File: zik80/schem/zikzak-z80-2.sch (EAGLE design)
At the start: 66 parts, among them IC1 Z80, IC10 74LS32N, IC11 74LS32N, IC12 74LS32N, IC13 74LS32N, IC14 74LS04N, IC15 74LS32N, IC16 ATMEGA644-20PU, IC2 ATMEGA644-20PU, IC3 MC6850, IC4 74LS32N, IC5 74LS04N, IC6 74LS32N, U2 FT232RLSSOP, X2 USB-SMD-NS

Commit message: Schematic update
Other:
- note added: "TODO: Check if VBL is needed.. VSYNC may be sufficient, and can be connected to both VGA and to IO mcu.. --> free a pin!"
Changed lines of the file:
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@@
 <setting verticaltext="up"/>
 </settings>
-<grid distance="0.05" unitdist="inch" unit="inch" style="dots" multiple="1" display="yes" altdistance="0.01" altunitdist="inch" altunit="inch"/>
+<grid distance="0.1" unitdist="inch" unit="inch" style="lines" multiple="1" display="no" altdistance="0.01" altunitdist="inch" altunit="inch"/>
 <layers>
 <layer number="1" name="Top" color="4" fill="1" visible="no" active="no"/>
@@
 <rectangle x1="3.81" y1="109.22" x2="35.56" y2="135.89" layer="203"/>
 <text x="6.35" y="138.43" size="5.08" layer="91">ISP Progr. IO</text>
+<text x="478.79" y="40.64" size="3.81" layer="94">TODO: Check if VBL is needed..
+VSYNC may be sufficient, and can be
+connected to both VGA and to IO mcu..
+--&gt; free a pin!</text>
 </plain>
 <instances>

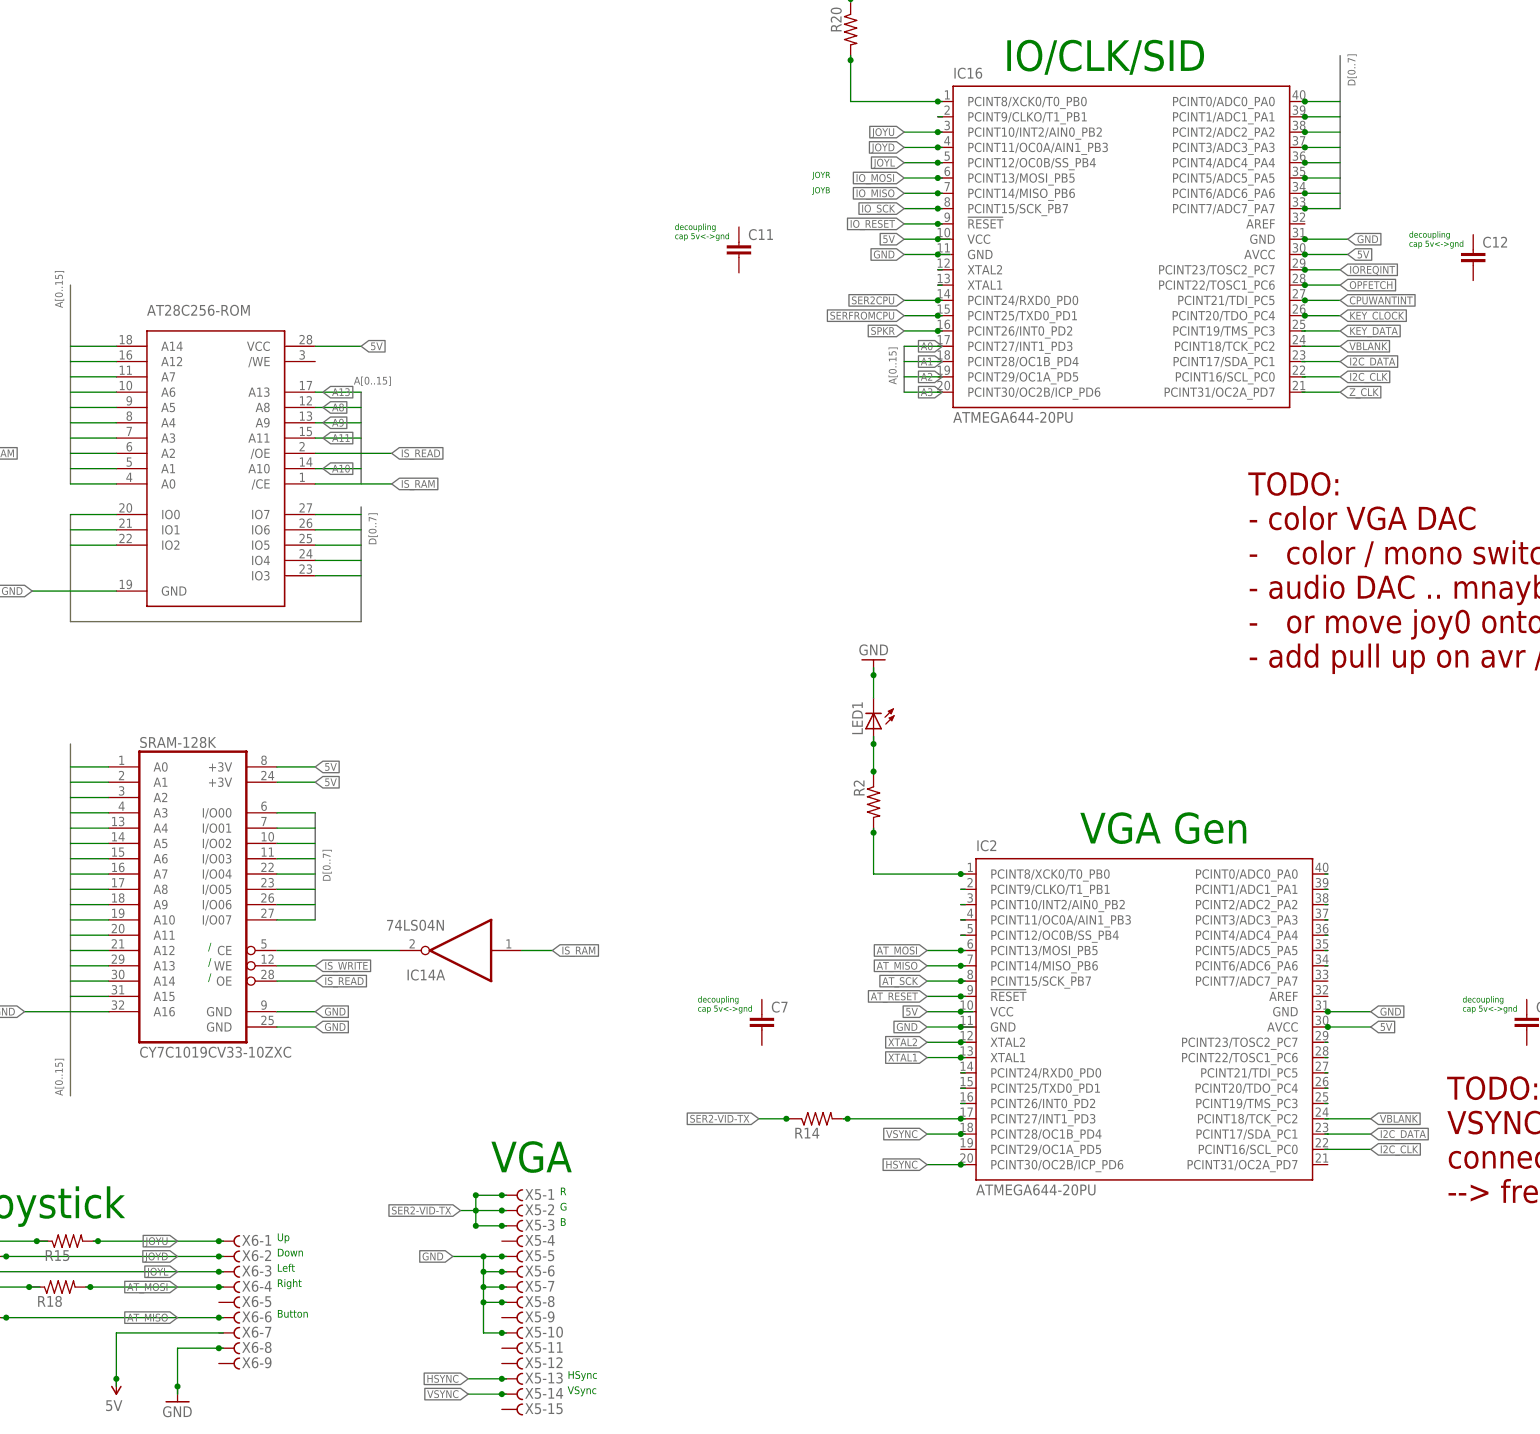
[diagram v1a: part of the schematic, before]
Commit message: Added skeleton for '3w' 3-wire-interface, but not using it; updated schem to move VGA stuff more to one side, opening up full side for something else..
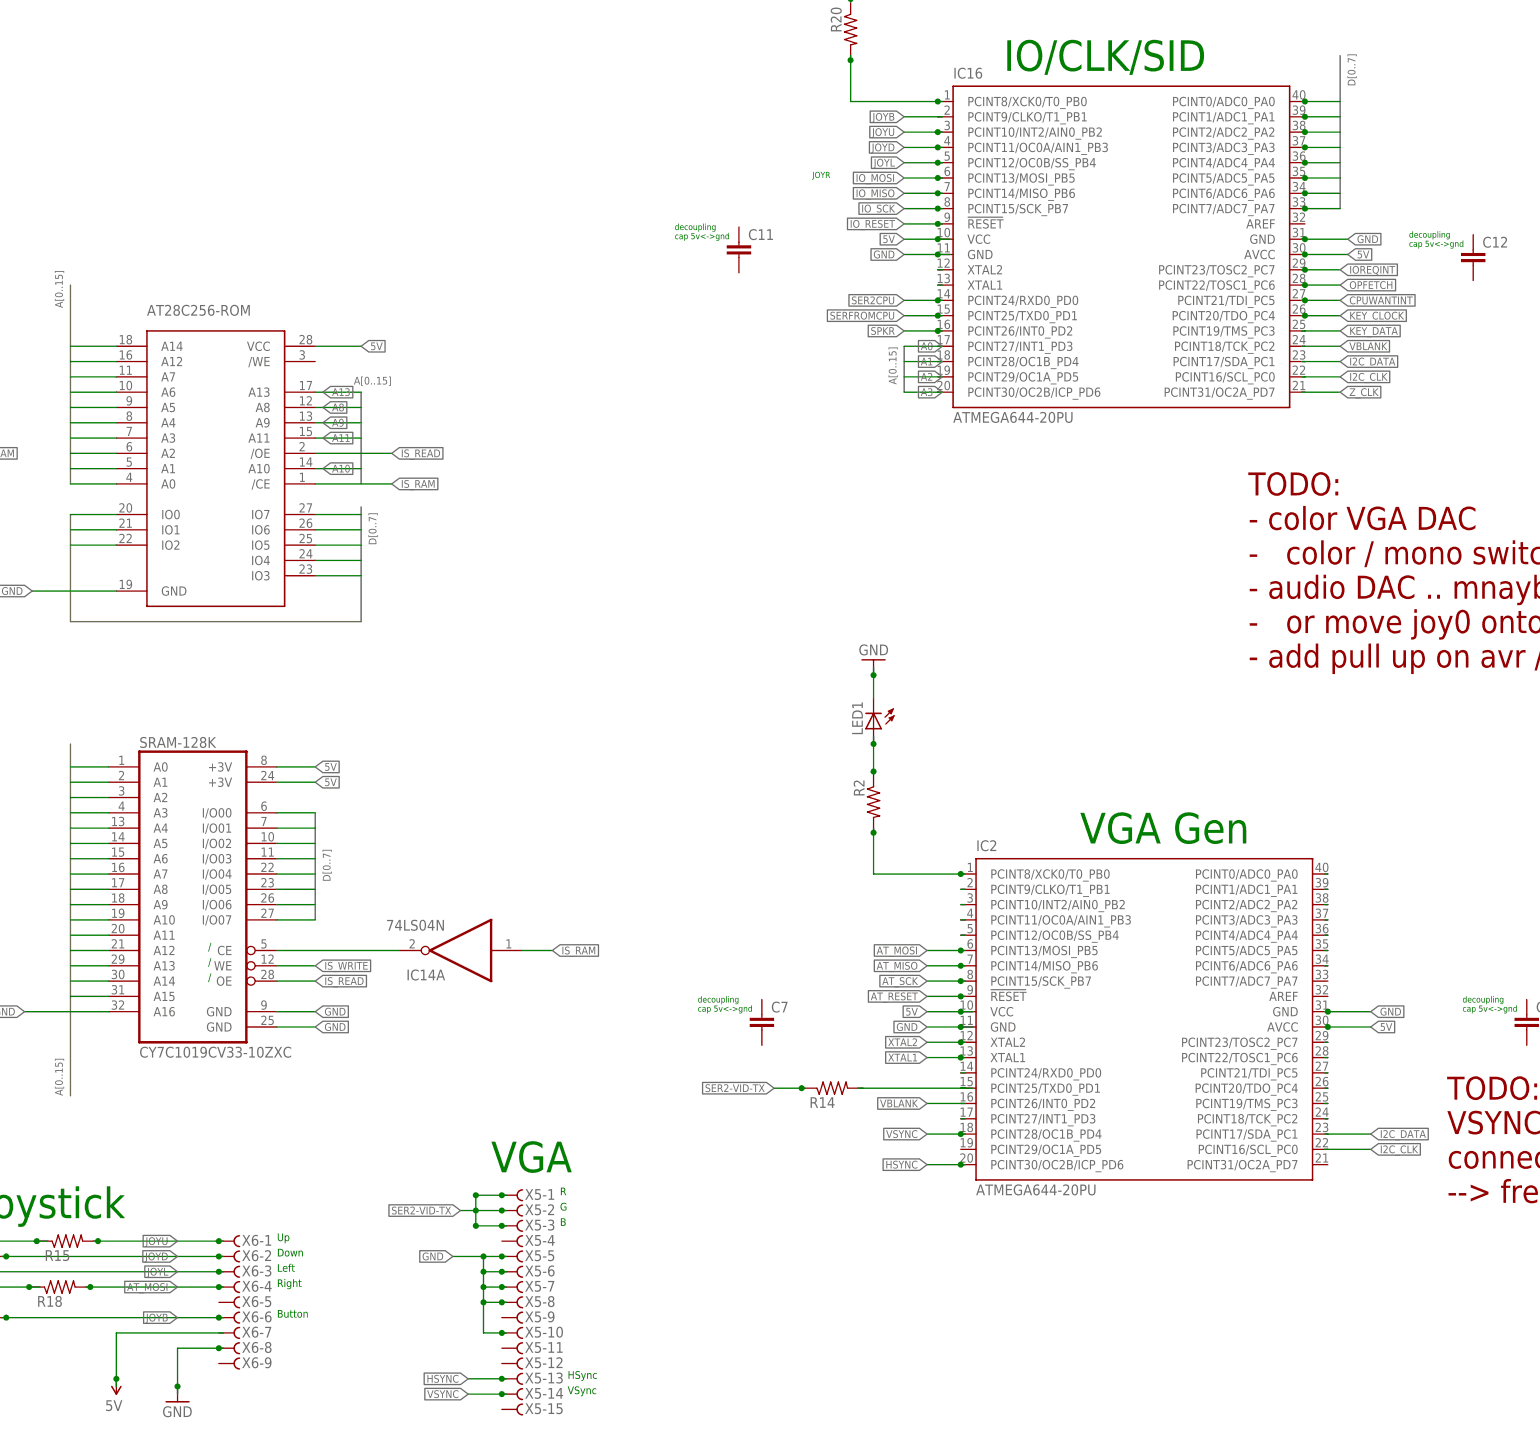
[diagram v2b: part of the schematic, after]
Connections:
- removed net N$13: IC16.PCINT8/XCK0/T0_PB0, R20.2
- new net JOYB: IC16.PCINT8/XCK0/T0_PB0, IC16.PCINT9/CLKO/T1_PB1, R19.2, R20.2, X6-6.F
- new net N$3: R14.2
- net AT_MISO: no longer R19.2, X6-6.F
- net CPUWANTINT: no longer IC16.PCINT9/CLKO/T1_PB1
- net N$10: no longer R14.2
- net SERFROMCPU: no longer IC2.PCINT25/TXD0_PD1
- net SPKR: no longer IC2.PCINT26/INT0_PD2
- net VBLANK: now also IC2.PCINT25/TXD0_PD1, IC2.PCINT26/INT0_PD2
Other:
- note removed: "JOYB"
- moved on the sheet: R14
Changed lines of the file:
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@@
 <setting verticaltext="up"/>
 </settings>
-<grid distance="0.1" unitdist="inch" unit="inch" style="lines" multiple="1" display="no" altdistance="0.01" altunitdist="inch" altunit="inch"/>
+<grid distance="0.05" unitdist="inch" unit="inch" style="dots" multiple="1" display="yes" altdistance="0.01" altunitdist="inch" altunit="inch"/>
 <layers>
 <layer number="1" name="Top" color="4" fill="1" visible="no" active="no"/>
@@
 cap 5v&lt;-&gt;gnd</text>
 <text x="373.38" y="210.82" size="1.016" layer="91">JOYR</text>
-<text x="373.38" y="208.28" size="1.016" layer="91">JOYB</text>
 <text x="472.44" y="199.39" size="1.016" layer="91">decoupling
 cap 5v&lt;-&gt;gnd</text>
@@
 <instance part="GND11" gate="1" x="78.74" y="8.89"/>
 <instance part="GND12" gate="1" x="93.98" y="8.89"/>
-<instance part="R14" gate="G$1" x="374.142" y="54.61" rot="MR180"/>
+<instance part="R14" gate="G$1" x="376.682" y="59.69" rot="MR180"/>
 <instance part="X6" gate="-1" x="277.368" y="34.29"/>
 <instance part="X6" gate="-2" x="277.368" y="31.75"/>
@@
 </segment>
 <segment>
-<wire x1="398.78" y1="59.69" x2="398.018" y2="59.69" width="0.1524" layer="91"/>
-<pinref part="IC2" gate="G$1" pin="PCINT25/TXD0_PD1"/>
-</segment>
-<segment>
 <wire x1="394.97" y1="187.96" x2="394.208" y2="187.96" width="0.1524" layer="91"/>
 <label x="388.62" y="187.96" size="1.27" layer="95" rot="R180" xref="yes"/>
@@
 <junction x="398.018" y="80.01"/>
 </segment>
-<segment>
-<wire x1="275.59" y1="21.59" x2="274.828" y2="21.59" width="0.1524" layer="91"/>
-<label x="267.97" y="21.59" size="1.27" layer="95" rot="R180" xref="yes"/>
-<wire x1="274.828" y1="21.59" x2="239.522" y2="21.59" width="0.1524" layer="91"/>
-<pinref part="X6" gate="-6" pin="F"/>
-<junction x="274.828" y="21.59"/>
-<pinref part="R19" gate="G$1" pin="2"/>
-<wire x1="239.522" y1="21.59" x2="238.76" y2="21.59" width="0.1524" layer="91"/>
-<junction x="239.522" y="21.59"/>
-</segment>
 </net>
 <net name="+5V" class="0">
@@
 </segment>
 <segment>
-<wire x1="394.97" y1="220.98" x2="394.208" y2="220.98" width="0.1524" layer="91"/>
-<pinref part="IC16" gate="G$1" pin="PCINT9/CLKO/T1_PB1"/>
-</segment>
-<segment>
 <wire x1="454.66" y1="190.5" x2="455.168" y2="190.5" width="0.1524" layer="91"/>
 <label x="461.01" y="190.5" size="1.27" layer="95" xref="yes"/>
@@
 <net name="N$10" class="0">
 <segment>
-<wire x1="378.46" y1="54.61" x2="379.222" y2="54.61" width="0.1524" layer="91"/>
 <pinref part="IC2" gate="G$1" pin="PCINT27/INT1_PD3"/>
-<wire x1="379.222" y1="54.61" x2="398.018" y2="54.61" width="0.1524" layer="91"/>
 <wire x1="398.018" y1="54.61" x2="398.78" y2="54.61" width="0.1524" layer="91"/>
-<junction x="398.018" y="54.61"/>
-<pinref part="R14" gate="G$1" pin="2"/>
-<junction x="379.222" y="54.61"/>
 </segment>
 </net>
@@
 <net name="SPKR" class="0">
 <segment>
-<wire x1="398.78" y1="57.15" x2="398.018" y2="57.15" width="0.1524" layer="91"/>
-<pinref part="IC2" gate="G$1" pin="PCINT26/INT0_PD2"/>
-</segment>
-<segment>
 <wire x1="148.59" y1="24.13" x2="147.32" y2="24.13" width="0.1524" layer="91"/>
 <wire x1="147.32" y1="24.13" x2="142.24" y2="24.13" width="0.1524" layer="91"/>
@@
 </segment>
 </net>
-<net name="N$13" class="0">
+<net name="JOYB" class="0">
 <segment>
 <wire x1="394.97" y1="223.52" x2="394.208" y2="223.52" width="0.1524" layer="91"/>
@@
 <junction x="379.73" y="230.378"/>
 </segment>
+<segment>
+<wire x1="394.97" y1="220.98" x2="394.208" y2="220.98" width="0.1524" layer="91"/>
+<pinref part="IC16" gate="G$1" pin="PCINT9/CLKO/T1_PB1"/>
+<wire x1="394.208" y1="220.98" x2="388.62" y2="220.98" width="0.1524" layer="91"/>
+<label x="388.62" y="220.98" size="1.27" layer="95" rot="R180" xref="yes"/>
+</segment>
+<segment>
+<wire x1="275.59" y1="21.59" x2="274.828" y2="21.59" width="0.1524" layer="91"/>
+<label x="267.97" y="21.59" size="1.27" layer="95" rot="R180" xref="yes"/>
+<wire x1="274.828" y1="21.59" x2="239.522" y2="21.59" width="0.1524" layer="91"/>
+<pinref part="X6" gate="-6" pin="F"/>
+<junction x="274.828" y="21.59"/>
+<pinref part="R19" gate="G$1" pin="2"/>
+<wire x1="239.522" y1="21.59" x2="238.76" y2="21.59" width="0.1524" layer="91"/>
+<junction x="239.522" y="21.59"/>
+</segment>
 </net>
 <net name="N$14" class="0">
@@
 <net name="SER2-VID-TX" class="0">
 <segment>
-<wire x1="369.57" y1="54.61" x2="369.062" y2="54.61" width="0.1524" layer="91"/>
-<label x="364.49" y="54.61" size="1.27" layer="95" rot="R180" xref="yes"/>
+<wire x1="372.11" y1="59.69" x2="371.602" y2="59.69" width="0.1524" layer="91"/>
+<label x="367.03" y="59.69" size="1.27" layer="95" rot="R180" xref="yes"/>
 <pinref part="R14" gate="G$1" pin="1"/>
-<wire x1="369.062" y1="54.61" x2="364.49" y2="54.61" width="0.1524" layer="91"/>
-<junction x="369.062" y="54.61"/>
+<wire x1="371.602" y1="59.69" x2="367.03" y2="59.69" width="0.1524" layer="91"/>
+<junction x="371.602" y="59.69"/>
 </segment>
 <segment>
@@
 <pinref part="IC2" gate="G$1" pin="PCINT18/TCK_PC2"/>
 <wire x1="458.978" y1="54.61" x2="458.47" y2="54.61" width="0.1524" layer="91"/>
-<wire x1="458.978" y1="54.61" x2="466.09" y2="54.61" width="0.1524" layer="91"/>
-<label x="466.09" y="54.61" size="1.27" layer="95" xref="yes"/>
 </segment>
 <segment>
@@
 <label x="461.01" y="182.88" size="1.27" layer="95" xref="yes"/>
 </segment>
-</net>
+<segment>
+<wire x1="398.78" y1="59.69" x2="398.018" y2="59.69" width="0.1524" layer="91"/>
+<pinref part="IC2" gate="G$1" pin="PCINT25/TXD0_PD1"/>
+</segment>
+<segment>
+<wire x1="398.78" y1="57.15" x2="398.018" y2="57.15" width="0.1524" layer="91"/>
+<pinref part="IC2" gate="G$1" pin="PCINT26/INT0_PD2"/>
+<wire x1="398.018" y1="57.15" x2="392.43" y2="57.15" width="0.1524" layer="91"/>
+<label x="392.43" y="57.15" size="1.27" layer="95" rot="R180" xref="yes"/>
+</segment>
+</net>
+<net name="N$3" class="0">
+<segment>
+<wire x1="381" y1="59.69" x2="381.762" y2="59.69" width="0.1524" layer="91"/>
+<pinref part="R14" gate="G$1" pin="2"/>
+<wire x1="381.762" y1="59.69" x2="398.78" y2="59.69" width="0.1524" layer="91"/>
+<wire x1="400.05" y1="59.69" x2="398.78" y2="59.69" width="0.1524" layer="91"/>
+</segment>
+</net>

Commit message: updated schem
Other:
- note added: "TODO: - color VGA DAC - color / mono switch via buffer IC? - audio DAC .. mnaybe via Shift Register? - or move joy0 onto shift-reg? - add pull up on avr /RESET * 2 - clock drive both mcus? or clkout on VGA to drive IO?"
- note removed: "TODO: - color VGA DAC - color / mono switch via buffer IC? - audio DAC .. mnaybe via Shift Register? - or move joy0 onto shift-reg? - add pull up on avr /RESET * 2"
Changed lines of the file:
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@@
 <setting verticaltext="up"/>
 </settings>
-<grid distance="0.05" unitdist="inch" unit="inch" style="dots" multiple="1" display="yes" altdistance="0.01" altunitdist="inch" altunit="inch"/>
+<grid distance="0.1" unitdist="inch" unit="inch" style="lines" multiple="1" display="no" altdistance="0.01" altunitdist="inch" altunit="inch"/>
 <layers>
 <layer number="1" name="Top" color="4" fill="1" visible="no" active="no"/>
@@
 - audio DAC .. mnaybe via Shift Register?
 -   or move joy0 onto shift-reg?
-- add pull up on avr /RESET * 2</text>
+- add pull up on avr /RESET * 2
+- clock drive both mcus? or clkout on VGA to drive IO?</text>
 <rectangle x1="3.81" y1="109.22" x2="35.56" y2="135.89" layer="203"/>
 <text x="6.35" y="138.43" size="5.08" layer="91">ISP Progr. IO</text>
